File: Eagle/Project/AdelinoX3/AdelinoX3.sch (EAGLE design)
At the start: 104 parts, among them J1 DC-044-A, J2 YELLOW-8P-2.54, J3 YELLOW-6P-2.54, J4 YELLOW-8P-2.54, J5 YELLOW-8P-2.54, J6 4P-2.0, J7 YELLOW-2X3P-2.54, J8 4P-2.0, Q1 NCE3407A, Q2 CJ2305, SW1 TS-1101F, U1 CJT1117-3.3, U2 MP1496DJ-SOT23-8, U3 ESP-12F / OPL: 317060163 / SM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, U4 DNP, U5 ATMEGA32U4-MUR-QFN44, U6 DNP, X1 306010049_XTAL_16MHZ-3225_4P

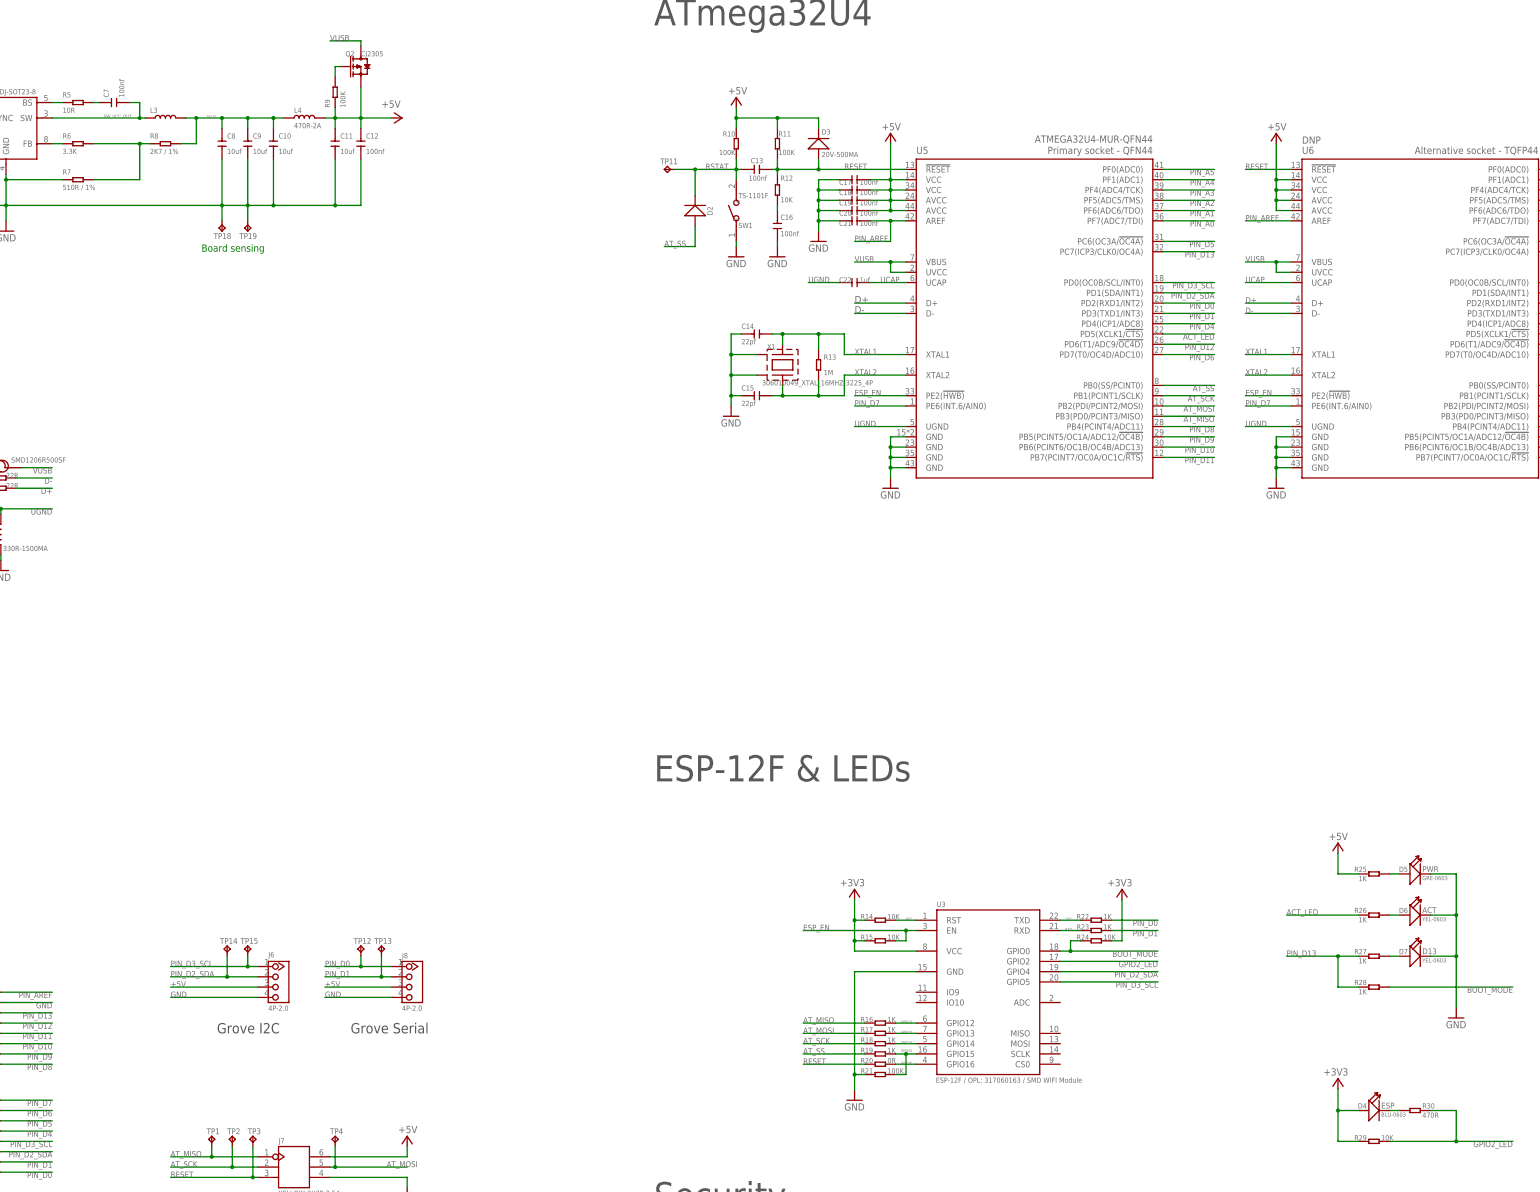
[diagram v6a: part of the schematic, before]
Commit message: Change bitmaps resolution to be more compatible.
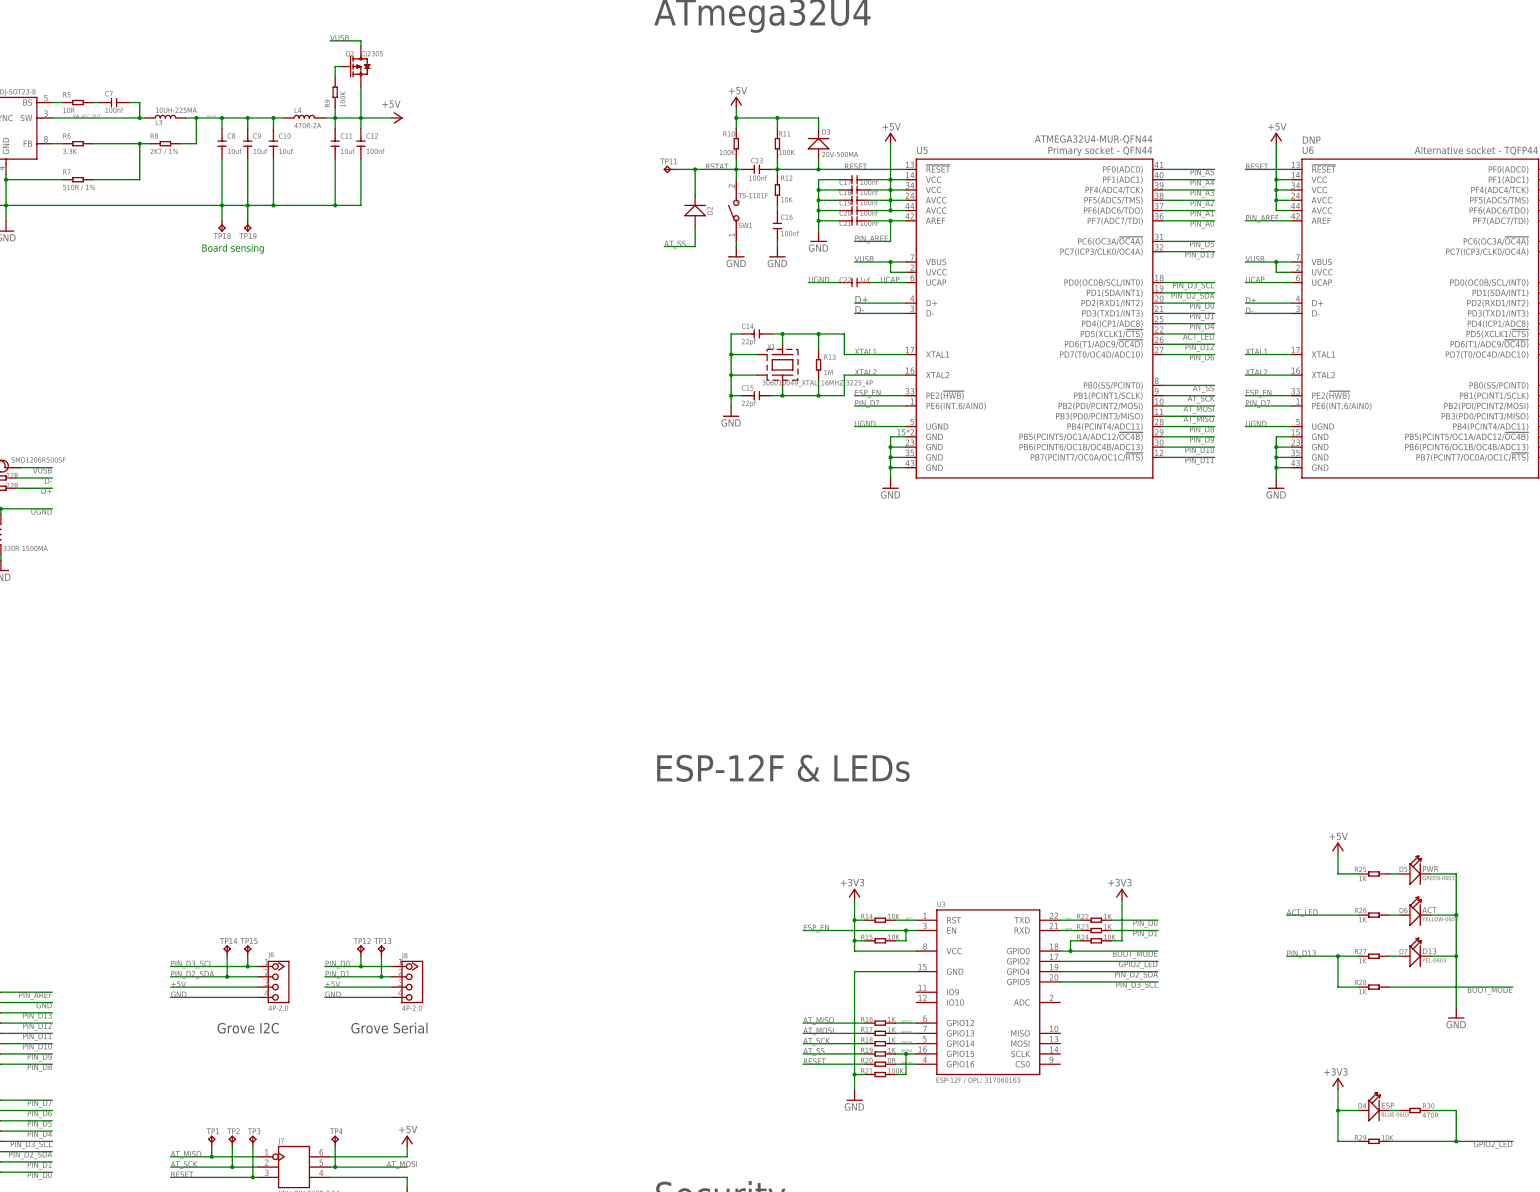
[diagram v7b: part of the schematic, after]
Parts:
- D4: value BLU-0603 -> BLUE-0603
- D5: value GRE-0603 -> GREEN-0603
- D6: value YEL-0603 -> YELLOW-0603
- U3: value ESP-12F / OPL: 317060163 / SMD WIFI Module -> ESP-12F / OPL: 317060163
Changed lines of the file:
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@@
 <attribute name="DESC" value="Primary socket - QFN44"/>
 </part>
-<part name="U3" library="Adelino-Misc" deviceset="ESP-12F" device="" value="ESP-12F / OPL: 317060163 / SMD WIFI Module"/>
+<part name="U3" library="Adelino-Misc" deviceset="ESP-12F" device="" value="ESP-12F / OPL: 317060163"/>
 <part name="USB1" library="Seeed-Connector" deviceset="MICRO-USB-SMD-B-WITHOUT-POST-W/P(ST-USB-001G)" device="" value="ST-USB-001G"/>
 <part name="J3" library="Seeed-Connector" deviceset="DIP-YELLOW-FEMALE-HEADER-VERT(6P-2.54)" device="" value="YELLOW-6P-2.54"/>
@@
 <part name="P+5" library="supply1" library_urn="urn:adsk.eagle:library:371" deviceset="+5V" device=""/>
 <part name="R14" library="Seeed-Resistor" deviceset="SMD-RES-10K-5%-1/10W(0603)" device="" value="10K"/>
-<part name="D4" library="Seeed-LED" deviceset="SMD-LED-CLEAR-BLUE(0603)" device="" value="BLU-0603">
+<part name="D4" library="Seeed-LED" deviceset="SMD-LED-CLEAR-BLUE(0603)" device="" value="BLUE-0603">
 <attribute name="LABEL" value="ESP"/>
 </part>
@@
 <part name="P+8" library="supply1" library_urn="urn:adsk.eagle:library:371" deviceset="+5V" device=""/>
 <part name="GND14" library="supply1" library_urn="urn:adsk.eagle:library:371" deviceset="GND" device=""/>
-<part name="D5" library="Seeed-LED" deviceset="SMD-LED-CLEAR-GREEN(0603)" device="" value="GRE-0603">
+<part name="D5" library="Seeed-LED" deviceset="SMD-LED-CLEAR-GREEN(0603)" device="" value="GREEN-0603">
 <attribute name="LABEL" value="PWR"/>
 </part>
-<part name="D6" library="Seeed-LED" deviceset="SMD-LED-CLEAR-YELLOW(0603)" device="" value="YEL-0603">
+<part name="D6" library="Seeed-LED" deviceset="SMD-LED-CLEAR-YELLOW(0603)" device="" value="YELLOW-0603">
 <attribute name="LABEL" value="ACT"/>
 </part>
@@
 </instance>
 <instance part="C7" gate="G$1" x="-119.38" y="147.32" smashed="yes" rot="R180">
-<attribute name="NAME" x="-120.65" y="148.59" size="1.27" layer="95" ratio="10" rot="R90"/>
-<attribute name="VALUE" x="-116.84" y="148.59" size="1.27" layer="96" ratio="10" rot="R90"/>
+<attribute name="NAME" x="-121.666" y="148.844" size="1.27" layer="95" ratio="10"/>
+<attribute name="VALUE" x="-121.666" y="144.78" size="1.27" layer="96" ratio="10"/>
 </instance>
 <instance part="L3" gate="G$1" x="-106.68" y="143.51" smashed="yes">
-<attribute name="NAME" x="-110.49" y="144.78" size="1.27" layer="95" ratio="10"/>
+<attribute name="NAME" x="-109.22" y="141.732" size="1.27" layer="95" ratio="10"/>
+<attribute name="VALUE" x="-109.22" y="144.78" size="1.27" layer="96" ratio="10"/>
 </instance>
 <instance part="R1" gate="G$1" x="-171.45" y="140.97" smashed="yes" rot="R270">
@@
 <wire x1="-113.03" y1="147.32" x2="-113.03" y2="143.51" width="0.1524" layer="91"/>
 <junction x="-113.03" y="143.51"/>
-<label x="-121.92" y="143.51" size="0.8128" layer="95"/>
-</segment>
-</net>
+<label x="-129.54" y="143.51" size="0.8128" layer="95"/>
+</segment>
+</net>
